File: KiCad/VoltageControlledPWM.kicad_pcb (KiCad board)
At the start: 2 copper layers, 74.8 x 48.5 mm, 26 parts, among them J1 +12V|GND|-12V, J2 3.3V|5.0V (Output Reference), J3 3.3V | 5.0V Voltage Control, J4 PWM Output, Q1 2N3906, U1 LM393, U2 CA3240E, U3 LM311

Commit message: Latest updates
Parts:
- added TP0: GND, TestPoint:TestPoint_Loop_D2.50mm_Drill1.0mm, F.Cu at (101.2, 103.6)
- added TP1: Square Wave, TestPoint:TestPoint_Loop_D2.50mm_Drill1.0mm, F.Cu at (108.5, 81.8)
- added TP2: Triange Wave, TestPoint:TestPoint_Loop_D2.50mm_Drill1.0mm, F.Cu at (128.7, 115.9)
- added TP3: Sweep, TestPoint:TestPoint_Loop_D2.50mm_Drill1.0mm, F.Cu at (132.8, 103.5)
- J1: value +12V|GND|-12V -> -12V | GND | +12V
- J2: value 3.3V|5.0V (Output Reference) -> 3.3V or 5.0V (Output Reference)
- J3: value 3.3V | 5.0V Voltage Control -> 3.3V or 5.0V Voltage Control
- R6: value 500 -> 460
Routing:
- net Net-(R1-Pad1): track 45.2 -> 49.9 mm
- net Net-(R10-Pad1): track 35.1 -> 39.1 mm
- net Net-(R8-Pad1): track 40.3 -> 36.7 mm

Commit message: Updated to the board.
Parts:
- R8: value 20K -> 27K
- R9: value 5K -> 10K
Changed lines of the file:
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@@
   (title_block
     (title "Voltage Controlled PWM")
-    (date 2021-07-17)
+    (date 2021-07-20)
     (rev V1.0)
     (company TetraSys)
@@
       (effects (font (size 1 1) (thickness 0.15)))
     )
-    (fp_text value 5K (at -0.1524 -1.5748 90) (layer F.SilkS)
+    (fp_text value 10K (at -0.1524 -1.5748 90) (layer F.SilkS)
       (effects (font (size 1 1) (thickness 0.15)))
     )
@@
       (effects (font (size 1 1) (thickness 0.15)))
     )
-    (fp_text value 20K (at 3.3528 0.4572) (layer F.SilkS)
+    (fp_text value 27K (at 3.3528 0.4572) (layer F.SilkS)
       (effects (font (size 1 1) (thickness 0.15)))
     )
@@
     (descr "8-lead though-hole mounted DIP package, row spacing 7.62 mm (300 mils)")
     (tags "THT DIP DIL PDIP 2.54mm 7.62mm 300mil")
-    (fp_text reference U3 (at 3.81 -1.7272 90) (layer F.SilkS)
-      (effects (font (size 1 1) (thickness 0.15)))
-    )
+    (fp_text reference U3 (at -2.032 3.9624 180) (layer F.SilkS)
+      (effects (font (size 1 1) (thickness 0.15)))
+    )

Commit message: Added Logos.
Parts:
- added G***: LOGO, TetraSysLogo:tetrasys-logo-8.4mm, B.Cu at (91.2, 97.7)
- added REF**: OSHW-Logo2_7.3x6mm_SilkScreen, Symbol:OSHW-Logo2_7.3x6mm_SilkScreen, B.Cu at (91.7, 88.5)
- added REF**: KiCad-Logo2_5mm_SilkScreen, Symbol:KiCad-Logo2_5mm_SilkScreen, B.Cu at (91.5, 110.3)

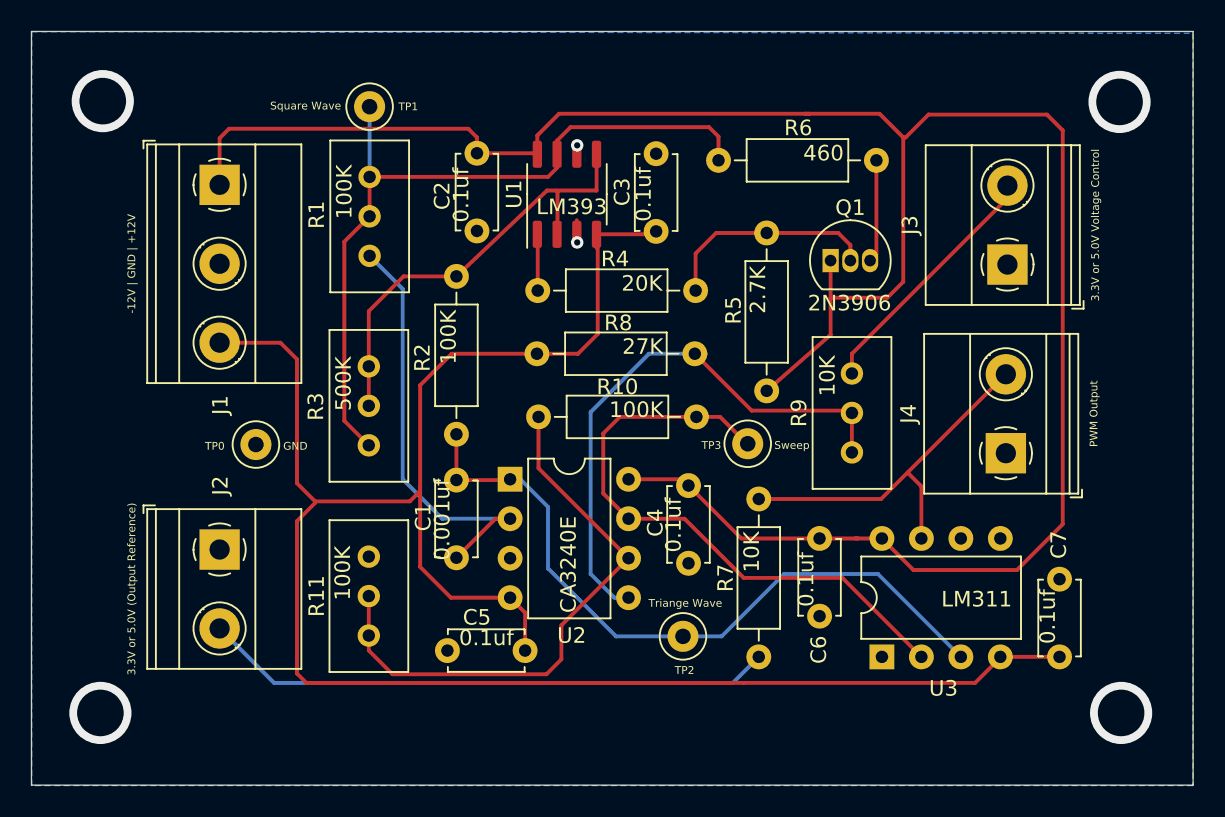
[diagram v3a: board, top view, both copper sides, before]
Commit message: Fixes for version 2.0. Changed the direction of increase voltage on R9 and R11. Increased silkscreen size of TPs.
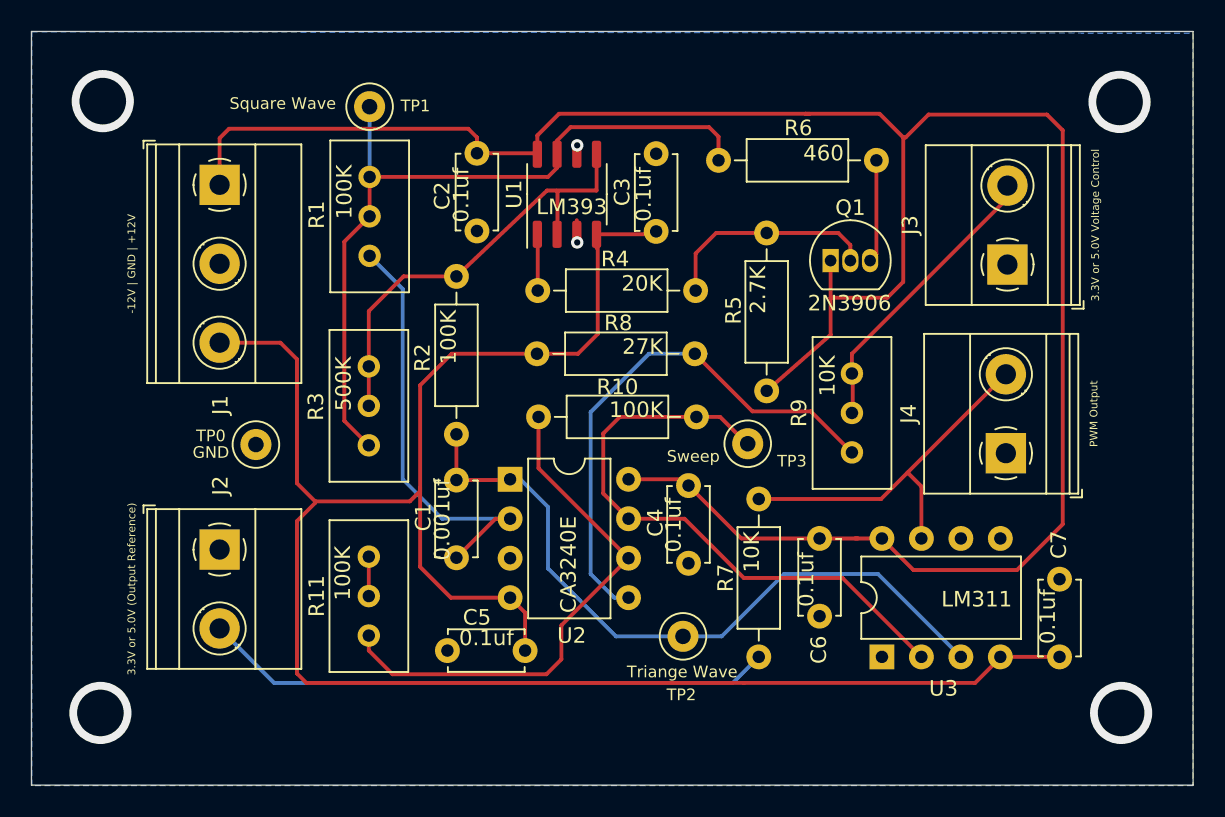
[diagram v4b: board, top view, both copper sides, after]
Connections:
- R11 pad 2: Net-(R10-Pad2) -> GND
- R9 pad 2: Net-(R8-Pad1) -> Net-(J3-Pad2)
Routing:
- net Net-(J3-Pad2): track 16.2 -> 19.0 mm
- net GND: track 1.51 -> 4.05 mm
- net Net-(R10-Pad2): track 36.7 -> 34.2 mm
- net Net-(R8-Pad1): track 36.7 -> 35.2 mm
